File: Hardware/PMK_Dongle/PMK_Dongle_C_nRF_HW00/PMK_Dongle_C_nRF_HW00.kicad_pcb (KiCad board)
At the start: 2 copper layers, 9.8 x 7.2 mm, 2 parts, among them J1 USB4151-GF-C, U1 BGA94C35P10X10_354X361X51

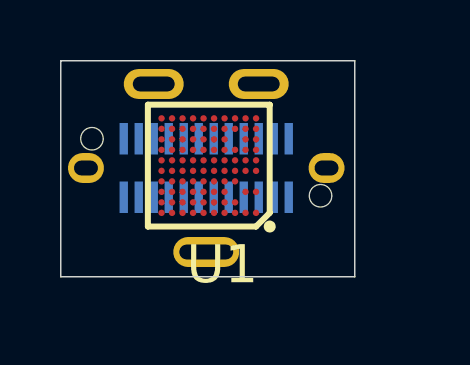
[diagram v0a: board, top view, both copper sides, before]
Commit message: started routing PMK_Dongle_C_NRF_00
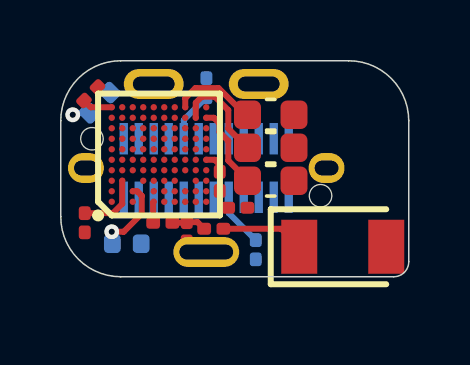
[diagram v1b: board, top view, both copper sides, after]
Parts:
- added ANT1: 2450AT18A100E, Component_lib:ANTC3216X140N, F.Cu at (181.8, 99.6)
- added C12: 100n, Capacitor_SMD:C_0201_0603Metric, F.Cu at (173.2, 98.8)
- added C14: 1u, Capacitor_SMD:C_0402_1005Metric, B.Cu at (173.7, 94.8)
- added C15: 1u, Capacitor_SMD:C_0402_1005Metric, B.Cu at (174.6, 99.5)
- added C19: 4u7, Capacitor_SMD:C_0603_1608Metric, F.Cu at (179.4, 96.3)
- added C20: 4u7, Capacitor_SMD:C_0603_1608Metric, F.Cu at (179.4, 97.4)
- added C3: 1p, Capacitor_SMD:C_0201_0603Metric, F.Cu at (176.6, 99.1)
- added C5: 100n, Capacitor_SMD:C_0201_0603Metric, F.Cu at (173.4, 94.5)
- added C6: 4u7, Capacitor_SMD:C_0603_1608Metric, F.Cu at (179.4, 95.2)
- added C7: 100n, Capacitor_SMD:C_0201_0603Metric, F.Cu at (177.7, 97.4)
- added C8: 100n, Capacitor_SMD:C_0201_0603Metric, F.Cu at (178.3, 98.3)
- added L1: 3n9, Inductor_SMD:L_0201_0603Metric, F.Cu at (175.8, 98.8)
- added L2: 4n7, Inductor_SMD:L_0201_0603Metric, F.Cu at (177.5, 99.0)
- added R1: 5k1, Resistor_SMD:R_0201_0603Metric, B.Cu at (177.3, 94.3)
- added R2: 5k1, Resistor_SMD:R_0201_0603Metric, B.Cu at (178.9, 99.7)
- U1: value BGA94C35P10X10_354X361X51 -> NRF52840-CKAA-F-R7
- moved U1 1.70 mm to (175.7, 96.5), turned to 90 degrees
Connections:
- J1 pad A1: Net-(J1-GND_1) -> GND
- J1 pad A12: Net-(J1-GND_1) -> GND
- J1 pad A4: Net-(J1-VBUS-PadA4) -> /VBUS
- J1 pad A5: unconnected-(J1-CC1-PadA5) -> /CC1
- J1 pad A6: unconnected-(J1-D+-PadA6) -> /D+
- J1 pad A7: unconnected-(J1-D--PadA7) -> /D-
- J1 pad A9: Net-(J1-VBUS-PadA4) -> /VBUS
- J1 pad B1: Net-(J1-GND_1) -> GND
- J1 pad B12: Net-(J1-GND_1) -> GND
- J1 pad B4: Net-(J1-VBUS-PadA4) -> /VBUS
- J1 pad B5: unconnected-(J1-CC2-PadB5) -> /CC2
- J1 pad B6: unconnected-(J1-D+-PadB6) -> /D+
- J1 pad B7: unconnected-(J1-D--PadB7) -> /D-
- J1 pad B9: Net-(J1-VBUS-PadA4) -> /VBUS
- J1 pad MH1: Net-(J1-MH2) -> GND
- J1 pad MH2: Net-(J1-MH2) -> GND
- J1 pad MH3: Net-(J1-MH2) -> GND
- J1 pad MH4: Net-(J1-MH2) -> GND
- J1 pad MH5: Net-(J1-MH2) -> GND
- U1 pad A10: unconnected-(U1-DEC1-PadA10) -> /DEC1
- U1 pad A8: unconnected-(U1-DEC4-PadA8) -> /DEC4
- U1 pad B3: unconnected-(U1-VDD_1-PadB3) -> /VDD_NRF
- U1 pad B7: unconnected-(U1-VSS_1-PadB7) -> GND
- U1 pad B8: unconnected-(U1-VDD_2-PadB8) -> /VDD_NRF
- U1 pad C1: unconnected-(U1-VSS_PA-PadC1) -> GND
- U1 pad C2: unconnected-(U1-DEC6-PadC2) -> /DEC4
- U1 pad C4: Net-(U1-VSS_10) -> GND
- U1 pad D3: Net-(U1-VSS_10) -> GND
- U1 pad D4: Net-(U1-VSS_10) -> GND
- U1 pad D5: Net-(U1-VSS_10) -> GND
- U1 pad D6: Net-(U1-VSS_10) -> GND
- U1 pad D7: Net-(U1-VSS_10) -> GND
- U1 pad D8: Net-(U1-VSS_10) -> GND
- U1 pad E1: unconnected-(U1-ANT-PadE1) -> Net-(U1-ANT)
- U1 pad E4: Net-(U1-VSS_10) -> GND
- U1 pad E5: Net-(U1-VSS_10) -> GND
- U1 pad E6: Net-(U1-VSS_10) -> GND
- U1 pad E7: Net-(U1-VSS_10) -> GND
- U1 pad E8: Net-(U1-VSS_10) -> GND
- U1 pad F4: Net-(U1-VSS_10) -> GND
- U1 pad F5: Net-(U1-VSS_10) -> GND
- U1 pad F6: Net-(U1-VSS_10) -> GND
- U1 pad F7: Net-(U1-VSS_10) -> GND
- U1 pad F8: Net-(U1-VSS_10) -> GND
- U1 pad G4: Net-(U1-VSS_10) -> GND
- U1 pad G5: Net-(U1-VSS_10) -> GND
- U1 pad G6: Net-(U1-VSS_10) -> GND
- U1 pad G7: Net-(U1-VSS_10) -> GND
- U1 pad G8: Net-(U1-VSS_10) -> GND
- U1 pad H10: unconnected-(U1-VDD_3-PadH10) -> /VDD_NRF
- U1 pad H2: unconnected-(U1-SWDCLK-PadH2) -> /SWDCLK
- U1 pad J10: unconnected-(U1-VDDH-PadJ10) -> /VBUS
- U1 pad J2: unconnected-(U1-SWDIO-PadJ2) -> /SWDIO
- U1 pad J8: unconnected-(U1-D--PadJ8) -> /D-
- U1 pad J9: unconnected-(U1-VBUS-PadJ9) -> /VBUS
- U1 pad K1: unconnected-(U1-VDD_4-PadK1) -> /VDD_NRF
- U1 pad K10: Net-(U1-VSS_10) -> GND
- U1 pad K5: unconnected-(U1-VDD_5-PadK5) -> /VDD_NRF
- U1 pad K8: unconnected-(U1-D+-PadK8) -> /D+
- U1 pad K9: unconnected-(U1-DECUSB-PadK9) -> Net-(U1-DECUSB)
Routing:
- net /VDD_NRF: track 0.00 -> 6.37 mm, vias 0 -> 1
- net /VBUS: track 0.00 -> 3.37 mm
- net Net-(U1-DECUSB): track 0.00 -> 2.82 mm
- net Net-(ANT1-A): track 0.00 -> 2.78 mm
- net /DEC4: track 0.00 -> 2.62 mm, vias 0 -> 1
- net /CC2: track 0.00 -> 1.80 mm
- net /CC1: track 0.00 -> 1.69 mm
- net Net-(C3-Pad1): track 0.00 -> 1.16 mm
- net /DEC1: track 0.00 -> 1.02 mm
- net Net-(U1-ANT): track 0.00 -> 0.71 mm
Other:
- board size 9.8 x 7.2 mm -> 11.6 x 7.2 mm
- copper layers 2 -> 6
